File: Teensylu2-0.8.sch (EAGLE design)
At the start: 113 parts, among them J1 12VPWR, J10 HOTEND-2, J11 E1-THRM, J12 B-THRM, J13 E2-THRM, J2 MICROSD, J3 USB-MICRO-PTH, J4 FAN, J5 4P-TERM-BLOCK284391-4, J6 39-29-3066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

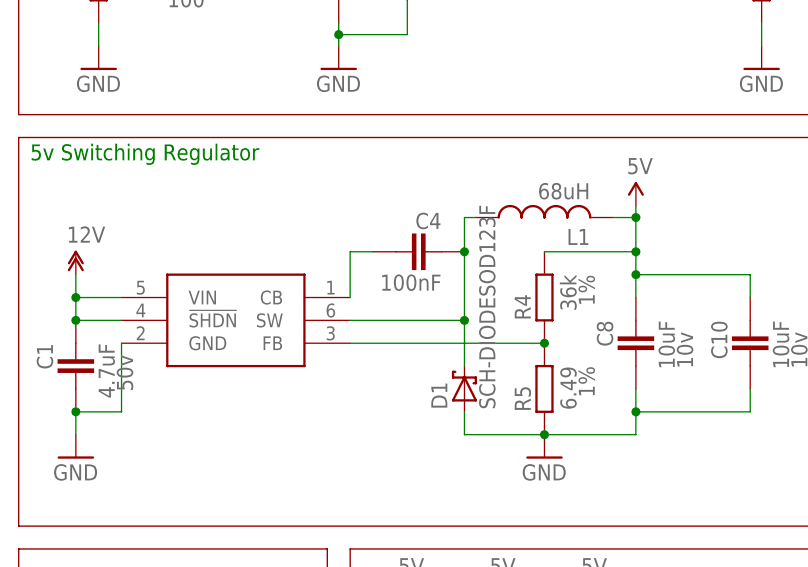
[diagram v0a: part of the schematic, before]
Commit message: Updated BOM
Added a BOM, changed C1 to 1206 package.
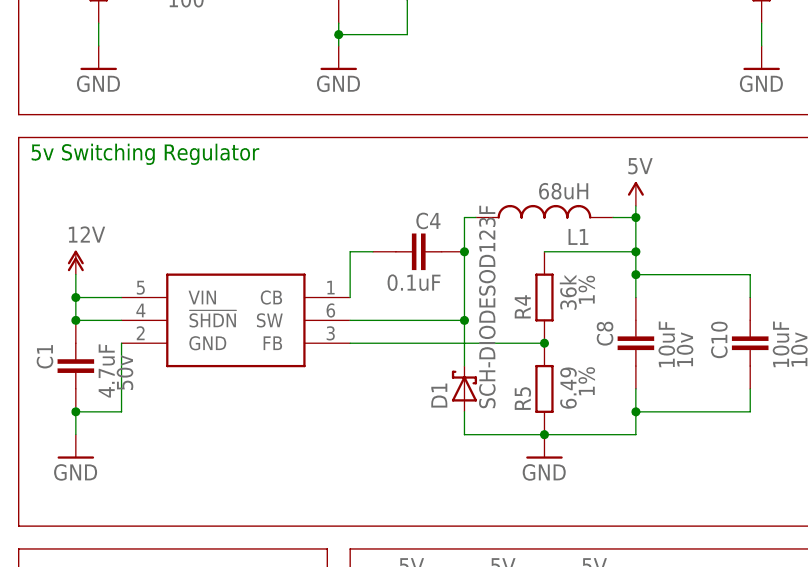
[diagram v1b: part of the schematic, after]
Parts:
- C1: device teensylu:CAPACITOR_0805 -> teensylu:CAPACITOR_1206; MANUFACTURER (none) -> Yaiyo Yuden; MANUFACTURER_PART_NUMBER (none) -> UMK316AB7475KL-T
- C10, C8: MANUFACTURER (none) -> Murata; MANUFACTURER_PART_NUMBER (none) -> GRM21BR71A106KE51L; TOLERANCE (none) -> 10%
- C11, C14, C15, C16: MANUFACTURER (none) -> Murata; MANUFACTURER_PART_NUMBER (none) -> GRM188R61C106MA73D; TOLERANCE (none) -> 20%; VOLTAGE (none) -> 16V
- C12, C13: MANUFACTURER (none) -> Samsung; MANUFACTURER_PART_NUMBER (none) -> CL10C100JB8NCNC; TOLERANCE (none) -> 5%; VOLTAGE (none) -> 50V
- C3, C7: MANUFACTURER (none) -> Murata; MANUFACTURER_PART_NUMBER (none) -> GRM188R71C104KA01D; TOLERANCE (none) -> 10%; VDC 10v -> 16v
- C4: value 100nF -> 0.1uF; ESR 0.0064 -> (none); MANUFACTURER (none) -> Samsung; MANUFACTURER_PART_NUMBER (none) -> CL10B104KB8NNNC; TOLERANCE (none) -> 10%; VDC 50 -> 50V
- C6: MANUFACTURER (none) -> Murata; MANUFACTURER_PART_NUMBER (none) -> GRM188R71C104KA01D; TOLERANCE (none) -> 10%; VDC 10v -> 16V
- C9: MANUFACTURER (none) -> Samsung; MANUFACTURER_PART_NUMBER (none) -> CL10A105MO8NNNC; TOLERANCE (none) -> 20%; VOLTAGE (none) -> 16
- LED1: MANUFACTURER (none) -> Kingbright; MANUFACTURER_PART_NUMBER (none) -> APT2012SGC
- U5: MANUFACTURER (none) -> Atmel; MANUFACTURER_PART_NUMBER (none) -> AT90USB1286
- X1: MANUFACTURER (none) -> NDK; MANUFACTURER_PART_NUMBER (none) -> NX5032GA-16.000000MHZ-LN-CD-1
